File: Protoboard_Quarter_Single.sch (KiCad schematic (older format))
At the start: 37 parts, among them P1 CONN_1, P10 CONN_1, P11 CONN_1, P12 CONN_1, P13 CONN_1, P14 CONN_1, P15 CONN_1, P16 CONN_1, P17 CONN_1, P18 CONN_1, P19 CONN_1, P20 CONN_1, P21 CONN_1, P22 CONN_1, P23 CONN_1, P24 CONN_1, P25 CONN_1, P26 CONN_1, P27 CONN_1, P28 CONN_1, P29 CONN_1, P3 CONN_1, P30 CONN_1, P31 CONN_1, P32 CONN_1, P33 CONN_1, P34 CONN_1, P35 CONN_1, P36 CONN_1, P38 CONN_1, P4 CONN_1, P5 CONN_1, P6 CONN_1, P7 CONN_1, P8 CONN_1, P9 CONN_1

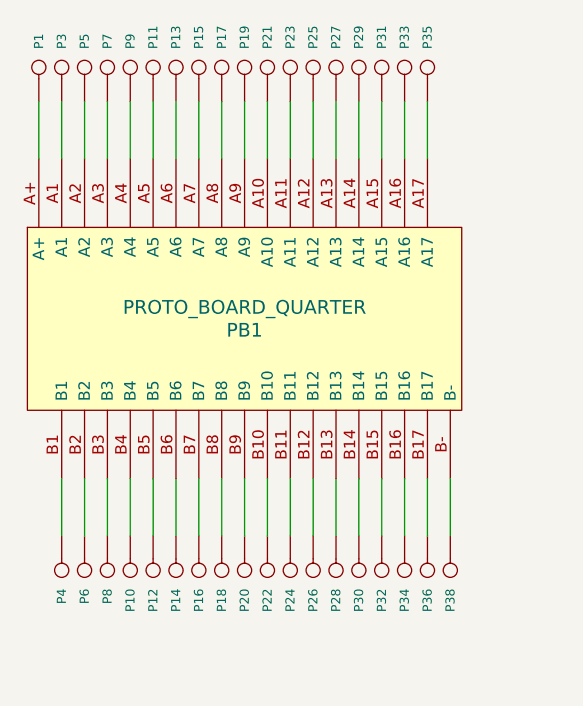
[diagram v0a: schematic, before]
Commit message: Change board size from 49.53mm X 44.20mm -> 48.25mm X 44.45mm Greatly increase track widths Minor silkscreen updates Add 1/8" mounting holes (1.7"/43.18mm apart)
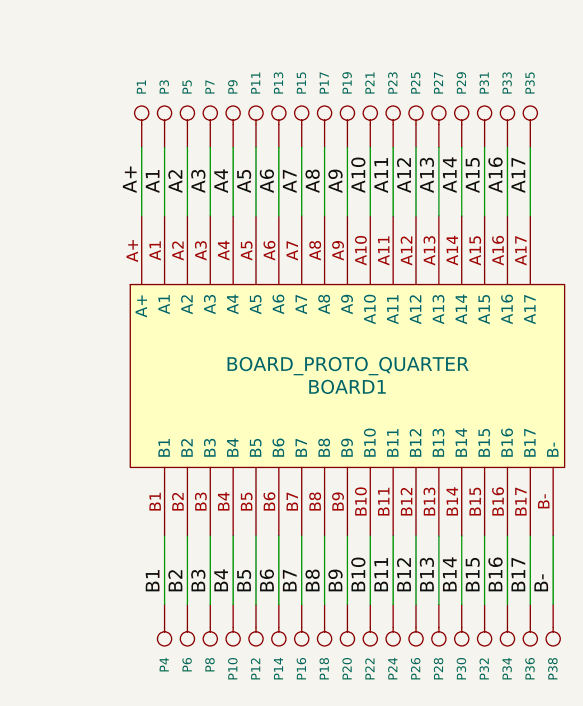
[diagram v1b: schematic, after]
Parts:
- removed PB1: PROTO_BOARD_QUARTER, symbol PROTO_BOARD_QUARTER
- added BOARD1: BOARD_PROTO_QUARTER, BOARD_PROTO_QUARTER, symbol BOARD_PROTO_QUARTER
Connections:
- net A+: now reaches P1.1
- net A+: now also BOARD1.A+
- net A1: now reaches P3.1
- net A1: now also BOARD1.A1
- net A10: now reaches P21.1
- net A10: now also BOARD1.A10
- net A11: now reaches P23.1
- net A11: now also BOARD1.A11
- net A12: now reaches P25.1
- net A12: now also BOARD1.A12
- net A13: now reaches P27.1
- net A13: now also BOARD1.A13
- net A14: now reaches P29.1
- net A14: now also BOARD1.A14
- net A15: now reaches P31.1
- net A15: now also BOARD1.A15
- net A16: now reaches P33.1
- net A16: now also BOARD1.A16
- net A17: now reaches P35.1
- net A17: now also BOARD1.A17
- net A2: now reaches P5.1
- net A2: now also BOARD1.A2
- net A3: now reaches P7.1
- net A3: now also BOARD1.A3
- net A4: now reaches P9.1
- net A4: now also BOARD1.A4
- net A5: now reaches P11.1
- net A5: now also BOARD1.A5
- net A6: now reaches P13.1
- net A6: now also BOARD1.A6
- net A7: now reaches P15.1
- net A7: now also BOARD1.A7
- net A8: now reaches P17.1
- net A8: now also BOARD1.A8
- net A9: now reaches P19.1
- net A9: now also BOARD1.A9
- net B-: now reaches P38.1
- net B-: now also BOARD1.B-
- net B1: now reaches P4.1
- net B1: now also BOARD1.B1
- net B10: now reaches P22.1
- net B10: now also BOARD1.B10
- net B11: now reaches P24.1
- net B11: now also BOARD1.B11
- net B12: now reaches P26.1
- net B12: now also BOARD1.B12
- net B13: now reaches P28.1
- net B13: now also BOARD1.B13
- net B14: now reaches P30.1
- net B14: now also BOARD1.B14
- net B15: now reaches P32.1
- net B15: now also BOARD1.B15
- net B16: now reaches P34.1
- net B16: now also BOARD1.B16
- net B17: now reaches P36.1
- net B17: now also BOARD1.B17
- net B2: now reaches P6.1
- net B2: now also BOARD1.B2
- net B3: now reaches P8.1
- net B3: now also BOARD1.B3
- net B4: now reaches P10.1
- net B4: now also BOARD1.B4
- net B5: now reaches P12.1
- net B5: now also BOARD1.B5
- net B6: now reaches P14.1
- net B6: now also BOARD1.B6
- net B7: now reaches P16.1
- net B7: now also BOARD1.B7
- net B8: now reaches P18.1
- net B8: now also BOARD1.B8
- net B9: now reaches P20.1
- net B9: now also BOARD1.B9
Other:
- moved on the sheet: P1, P10, P11, P12, P13, P14, P15, P16, P17, P18, P19, P20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
